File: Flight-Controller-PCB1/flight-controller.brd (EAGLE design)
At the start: 79.9 x 27.9 mm, 45 parts, among them J1 1981584-1, U1 MK20DX256VLH7, U2 TPS61200, U3 MINI54TAN, Y1 32.768KHz, Y2 16Mhz/8pF

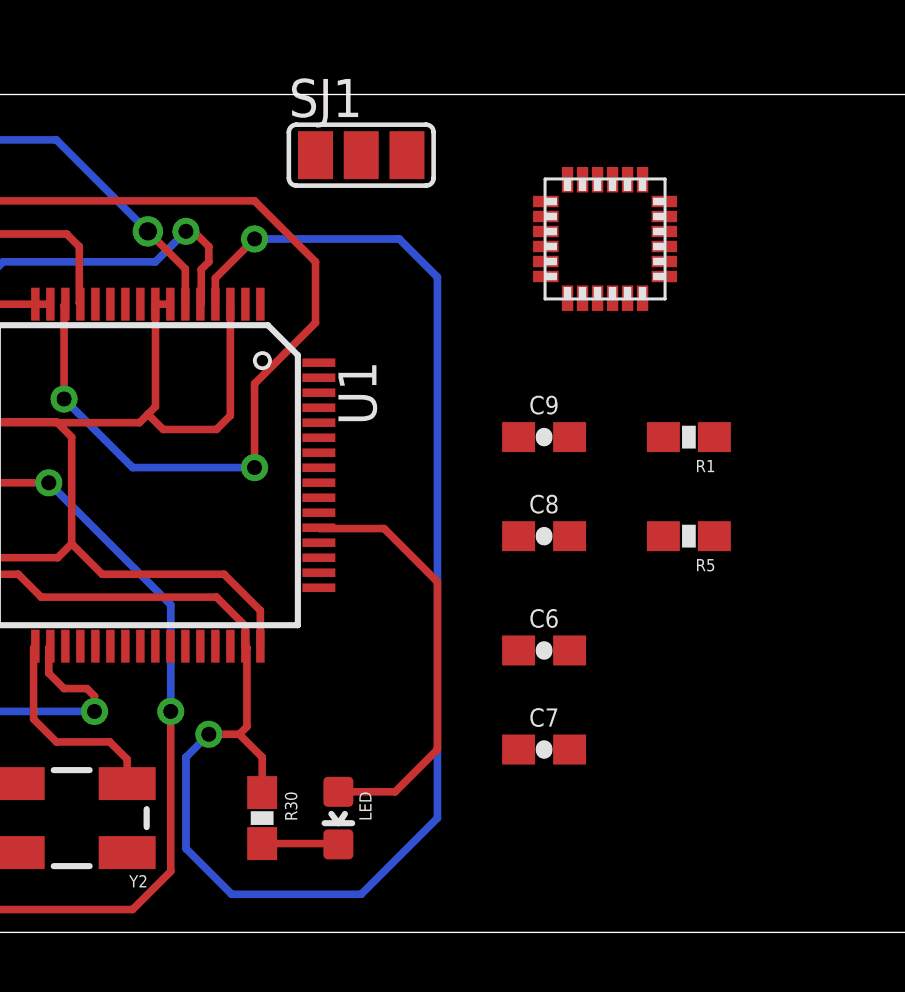
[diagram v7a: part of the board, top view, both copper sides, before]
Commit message: nearly finished routing the IMU
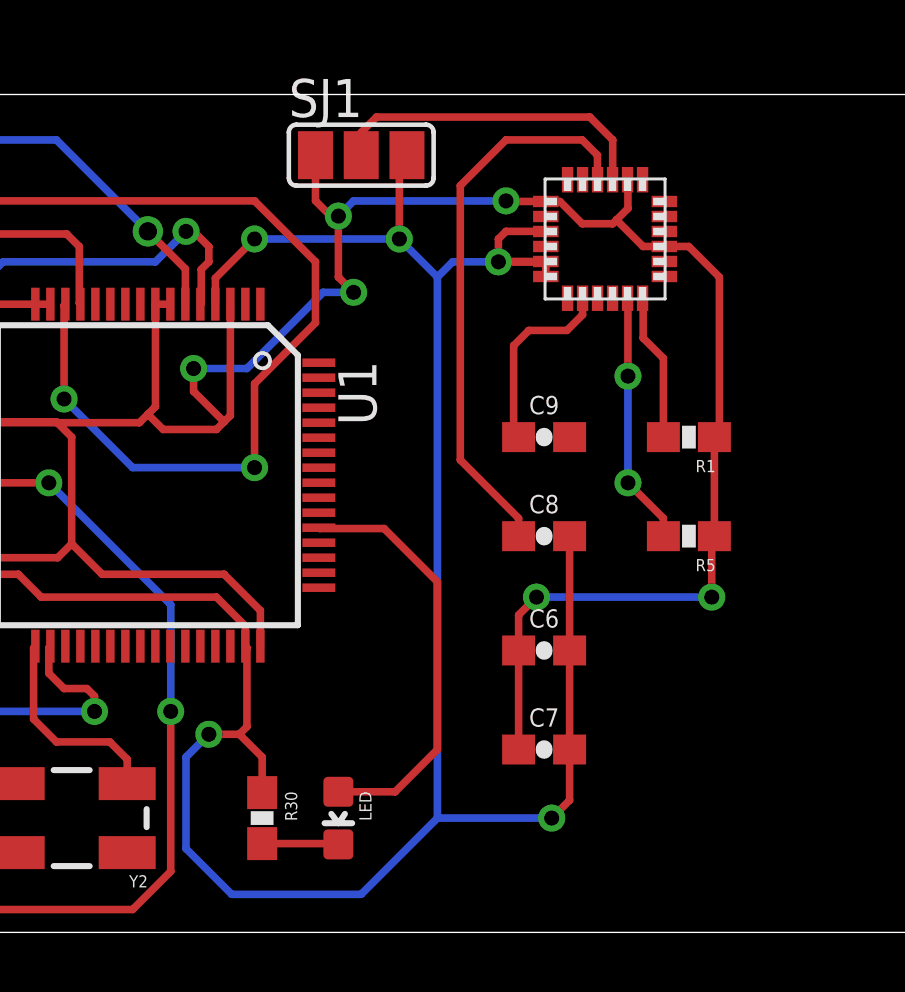
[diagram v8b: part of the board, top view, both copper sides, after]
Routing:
- net 3.3V: track 154.5 -> 206.5 mm, vias 5 -> 11
- net GND: track 198.5 -> 223.2 mm, vias 12 -> 15
- net N$4: track 0.00 -> 18.7 mm
- net N$5: track 0.00 -> 11.0 mm
- net SCL: track 0.00 -> 8.43 mm, vias 0 -> 2
- net N$3: track 0.00 -> 6.39 mm
- net SDA: track 0.00 -> 4.92 mm
